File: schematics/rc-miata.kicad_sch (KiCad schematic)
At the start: 5 parts, among them M1 BLDC_MOTOR, U1 ESP32-C3-DevKitM-1, U2 UBEC, U3 ESC

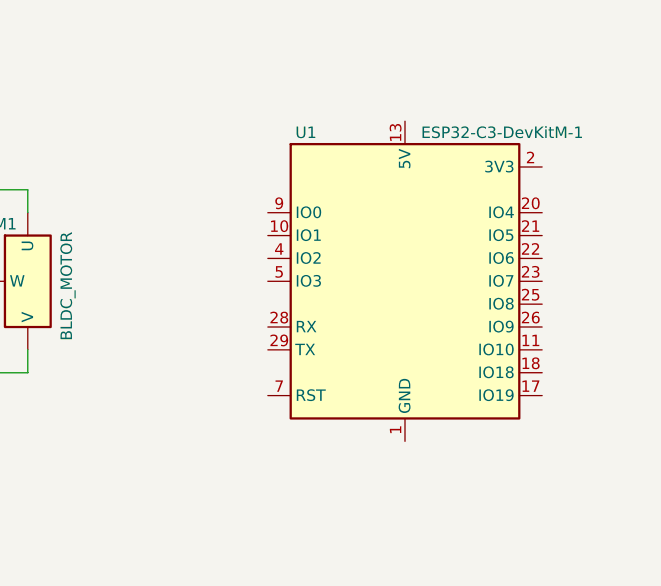
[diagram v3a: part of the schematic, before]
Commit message: Added 5V to ESP
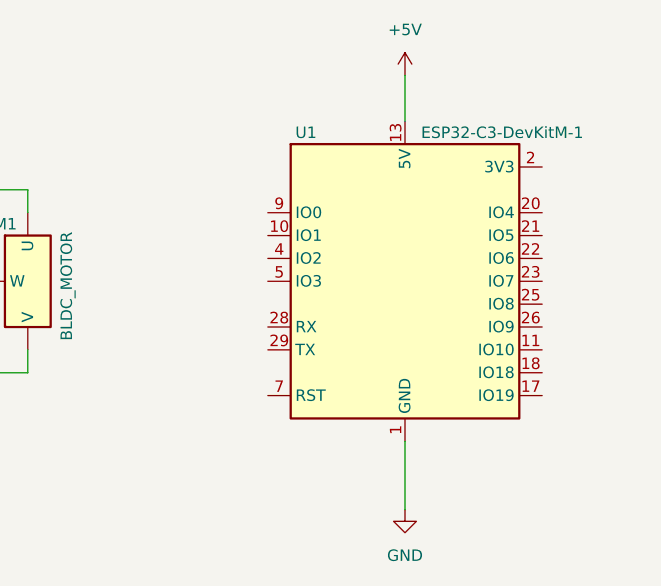
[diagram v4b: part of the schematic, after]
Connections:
- net +5V: now also U1.13 (5V), U1.14 (5V)
- net GND: now also U1.1 (GND), U1.12 (GND), U1.15 (GND), U1.16 (GND), U1.19 (GND), U1.24 (GND), U1.27 (GND), U1.30 (GND), U1.6 (GND), U1.8 (GND)
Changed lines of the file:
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@@
+	(wire
+		(pts
+			(xy 170.18 134.62) (xy 170.18 127)
+		)
+		(stroke
+			(width 0)
+			(type default)
+		)
+	)
 	(wire
 		(pts
@@
 		(pts
 			(xy 60.96 93.98) (xy 38.1 93.98)
+		)
+		(stroke
+			(width 0)
+			(type default)
+		)
+	)
+	(wire
+		(pts
+			(xy 170.18 86.36) (xy 170.18 91.44)
 		)
 		(stroke
@@
 	)
 	(symbol
+		(lib_id "power:GND")
+		(at 170.18 134.62 0)
+		(unit 1)
+		(body_style 1)
+		(exclude_from_sim no)
+		(in_bom yes)
+		(on_board yes)
+		(in_pos_files yes)
+		(dnp no)
+		(fields_autoplaced yes)
+		(property "Reference" "#PWR06"
+			(at 170.18 140.97 0)
+			(hide yes)
+			(show_name no)
+			(do_not_autoplace no)
+			(effects
+				(font
+					(size 1.27 1.27)
+				)
+			)
+		)
+		(property "Value" "GND"
+			(at 170.18 139.7 0)
+			(show_name no)
+			(do_not_autoplace no)
+			(effects
+				(font
+					(size 1.27 1.27)
+				)
+			)
+		)
+		(property "Footprint" ""
+			(at 170.18 134.62 0)
+			(hide yes)
+			(show_name no)
+			(do_not_autoplace no)
+			(effects
+				(font
+					(size 1.27 1.27)
+				)
+			)
+		)
+		(property "Datasheet" ""
+			(at 170.18 134.62 0)
+			(hide yes)
+			(show_name no)
+			(do_not_autoplace no)
+			(effects
+				(font
+					(size 1.27 1.27)
+				)
+			)
+		)
+		(property "Description" "Power symbol creates a global label with name \"GND\" , ground"
+			(at 170.18 134.62 0)
+			(hide yes)
+			(show_name no)
+			(do_not_autoplace no)
+			(effects
+				(font
+					(size 1.27 1.27)
+				)
+			)
+		)
+		(pin "1"
+		)
+		(instances
+			(project "rc-miata"
+				(path "/59cbdaad-7c89-4958-b9bb-08b035442600"
+					(reference "#PWR06")
+					(unit 1)
+				)
+			)
+		)
+	)
+	(symbol
 		(lib_id "RC Components:UBEC")
 		(at 58.42 101.6 0)
@@
 					(unit 1)
 				)
+			)
+		)
+	)
+	(symbol
+		(lib_id "power:+5V")
+		(at 170.18 86.36 0)
+		(unit 1)
+		(body_style 1)
+		(exclude_from_sim no)
+		(in_bom yes)
+		(on_board yes)
+		(in_pos_files yes)
+		(dnp no)
+		(fields_autoplaced yes)
+		(property "Reference" "#PWR05"
+			(at 170.18 90.17 0)
+			(hide yes)
+			(show_name no)
+			(do_not_autoplace no)
+			(effects
+				(font
+					(size 1.27 1.27)
+				)
+			)
+		)
+		(property "Value" "+5V"
+			(at 170.18 81.28 0)
+			(show_name no)
+			(do_not_autoplace no)
+			(effects
+				(font
+					(size 1.27 1.27)
+				)
+			)
+		)
+		(property "Footprint" ""
+			(at 170.18 86.36 0)
+			(hide yes)
+			(show_name no)
+			(do_not_autoplace no)
+			(effects
+				(font
+					(size 1.27 1.27)
+				)
+			)
+		)
+		(property "Datasheet" ""
+			(at 170.18 86.36 0)
+			(hide yes)
+			(show_name no)
+			(do_not_autoplace no)
+			(effects
+				(font
+					(size 1.27 1.27)
+				)
+			)
+		)
+		(property "Description" "Power symbol creates a global label with name \"+5V\""
+			(at 170.18 86.36 0)
+			(hide yes)
+			(show_name no)
+			(do_not_autoplace no)
+			(effects
+				(font
+					(size 1.27 1.27)
+				)
+			)
+		)
+		(pin "1"
+		)
+		(instances
+			(project "rc-miata"
+				(path "/59cbdaad-7c89-4958-b9bb-08b035442600"
+					(reference "#PWR05")
+					(unit 1)
+				)

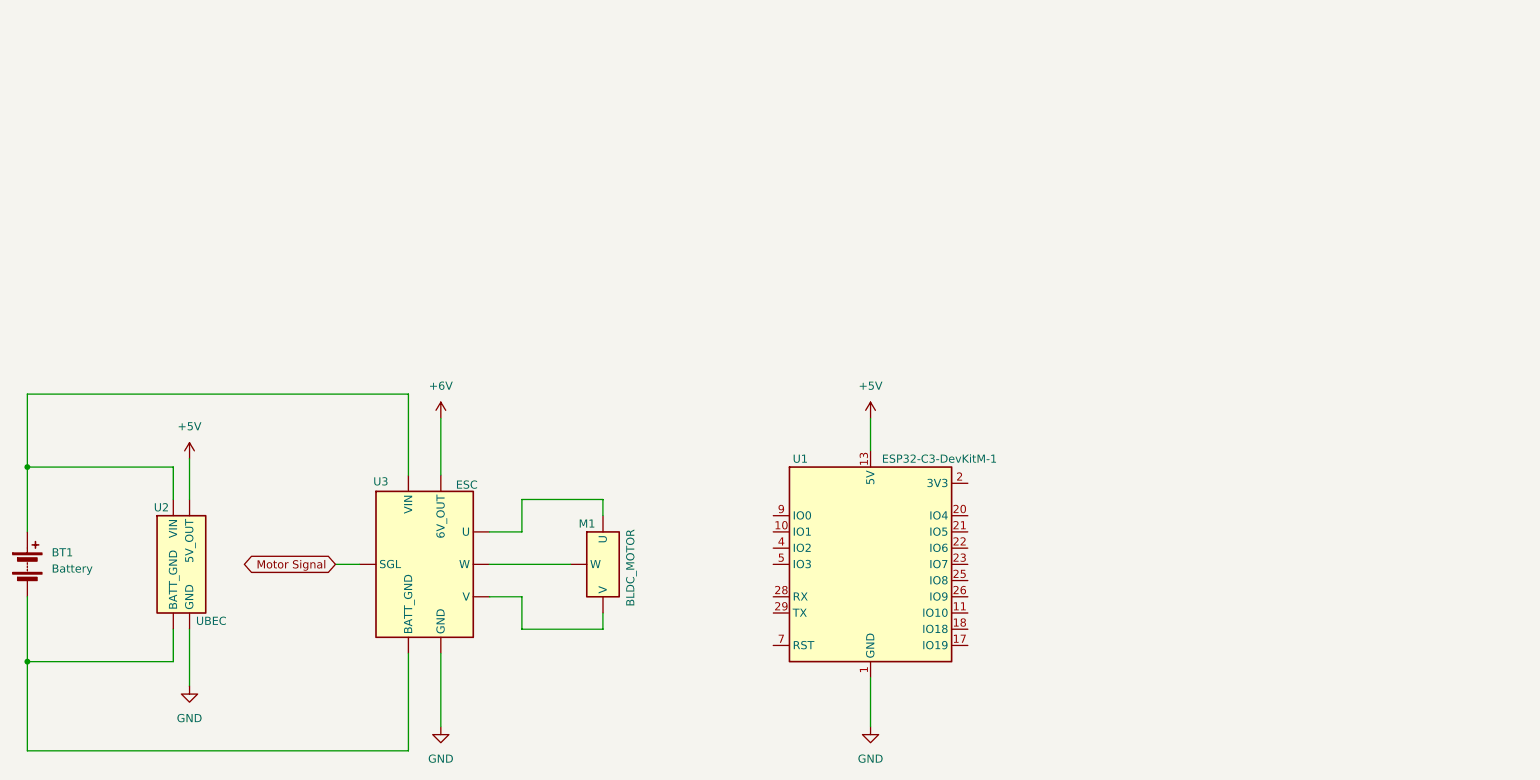
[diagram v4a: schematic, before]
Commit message: Named nets. Started updating ESP32
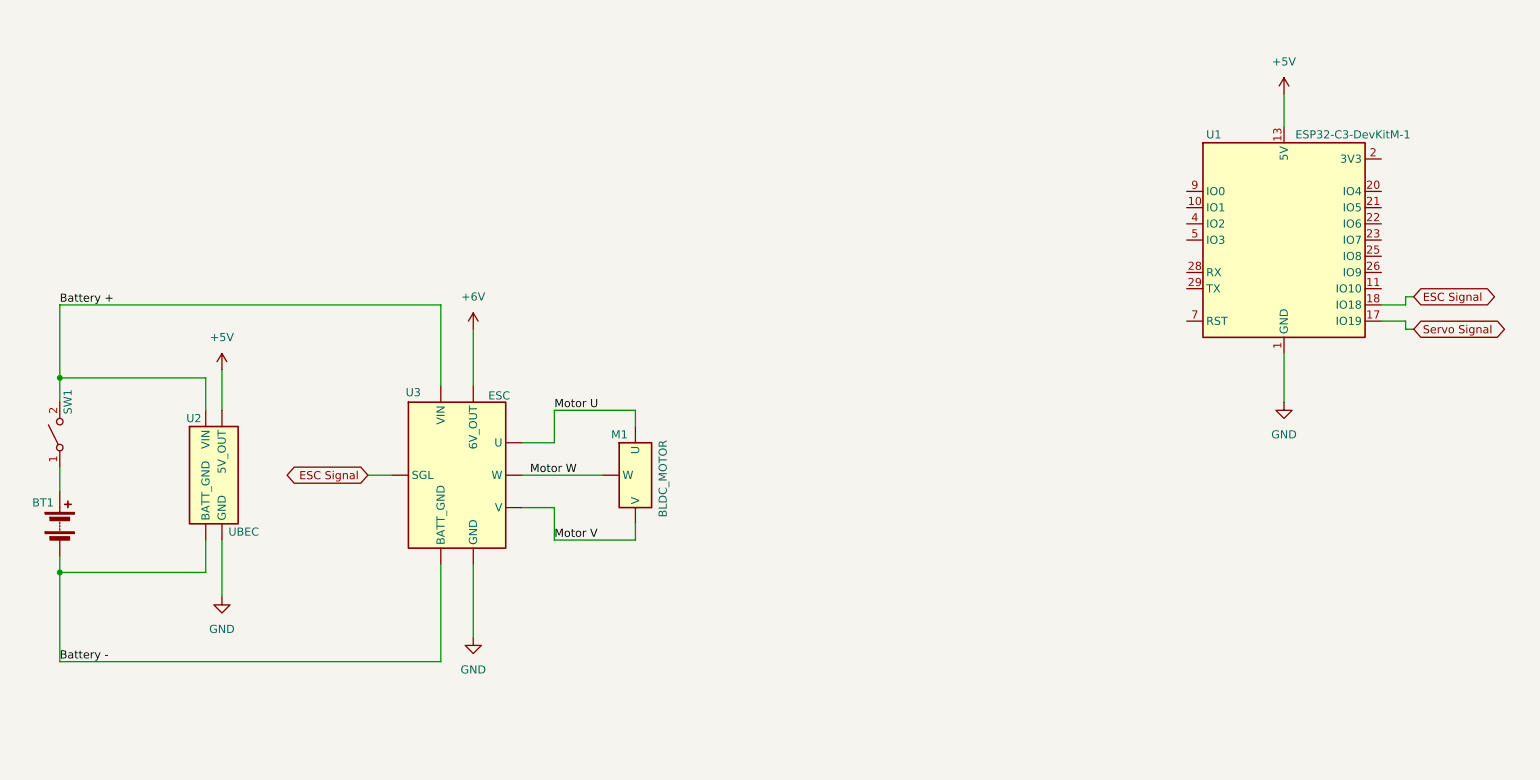
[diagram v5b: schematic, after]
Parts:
- added SW1: (no value), symbol Switch:SW_SPST
- BT1: value Battery -> 11.1
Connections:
- net Motor Signal is gone; now on net ESC Signal: U3.5 (SGL)
- net Servo Signal: now reaches U1.17 (IO19)
- net ESC Signal: now reaches U1.18 (IO18)
- net Motor U: now reaches M1.1 (U), U3.6 (U)
- net Motor V: now reaches M1.2 (V), U3.7 (V)
- net Motor W: now reaches M1.3 (W), U3.8 (W)
- net Battery +: now reaches U2.1 (VIN), U3.1 (VIN)
- net Battery +: now also SW1.2 (B); no longer BT1.1 (+)
- net Battery -: now reaches BT1.2 (-), U2.2 (BATT_GND), U3.2 (BATT_GND)
- new net: BT1.1 (+), SW1.1 (A)
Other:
- moved on the sheet: BT1, M1, U1, U2, U3

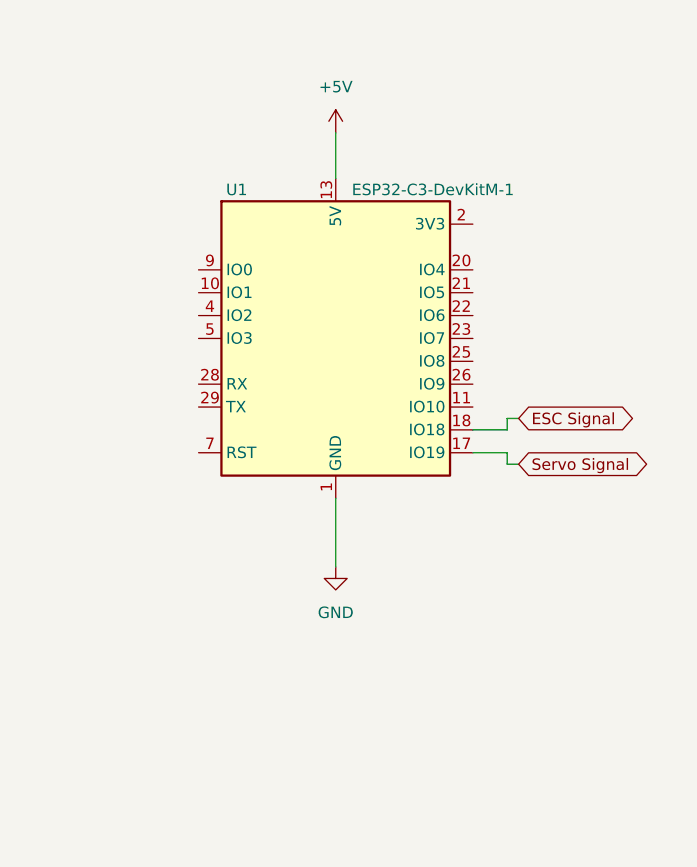
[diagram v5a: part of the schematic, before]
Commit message: Created ESP32 Symbol. Wired ESP32
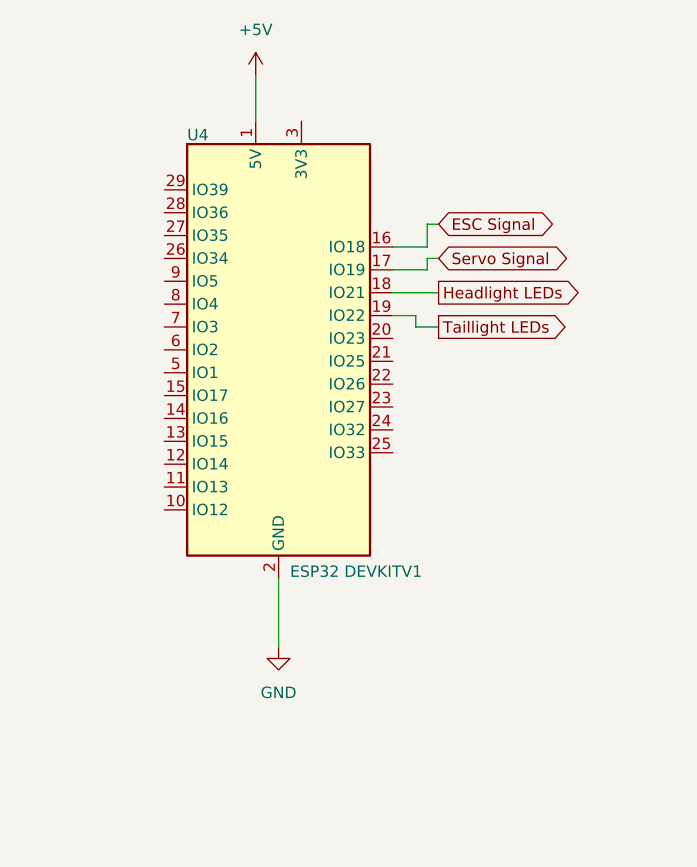
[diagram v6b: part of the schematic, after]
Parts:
- removed U1: ESP32-C3-DevKitM-1, RF_Module:ESP32-C3-DevKitM-1, symbol RF_Module:ESP32-C3-DevKitM-1
- added U4: ESP32 DEVKITV1, symbol ESP32s:ESP32_DEVKITV1
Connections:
- net +5V: now also U4.1 (5V)
- net ESC Signal: now also U4.16 (IO18)
- net GND: now also U4.2 (GND)
- net Servo Signal: now also U4.17 (IO19)
- new net Headlight LEDs: U4.18 (IO21)
- new net Taillight LEDs: U4.19 (IO22)

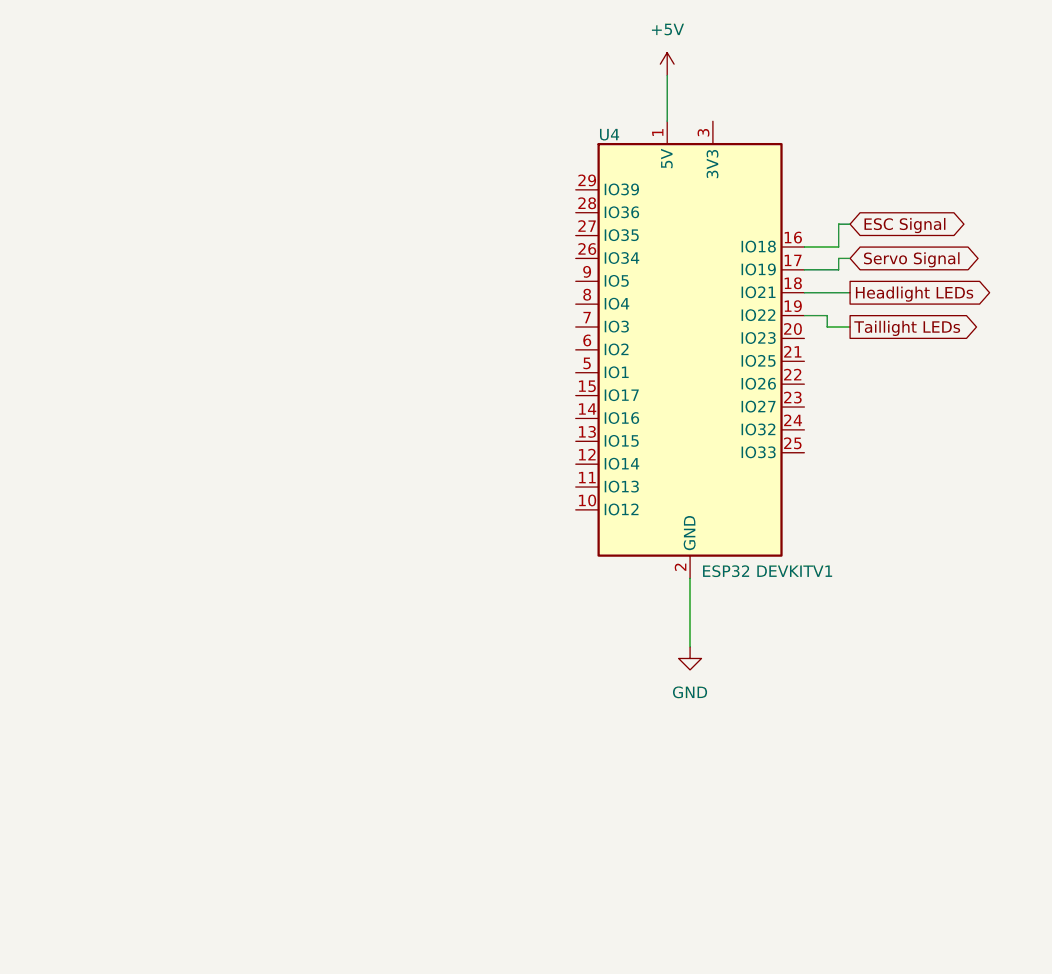
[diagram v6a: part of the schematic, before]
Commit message: Created Servo symbol. Wired servo.
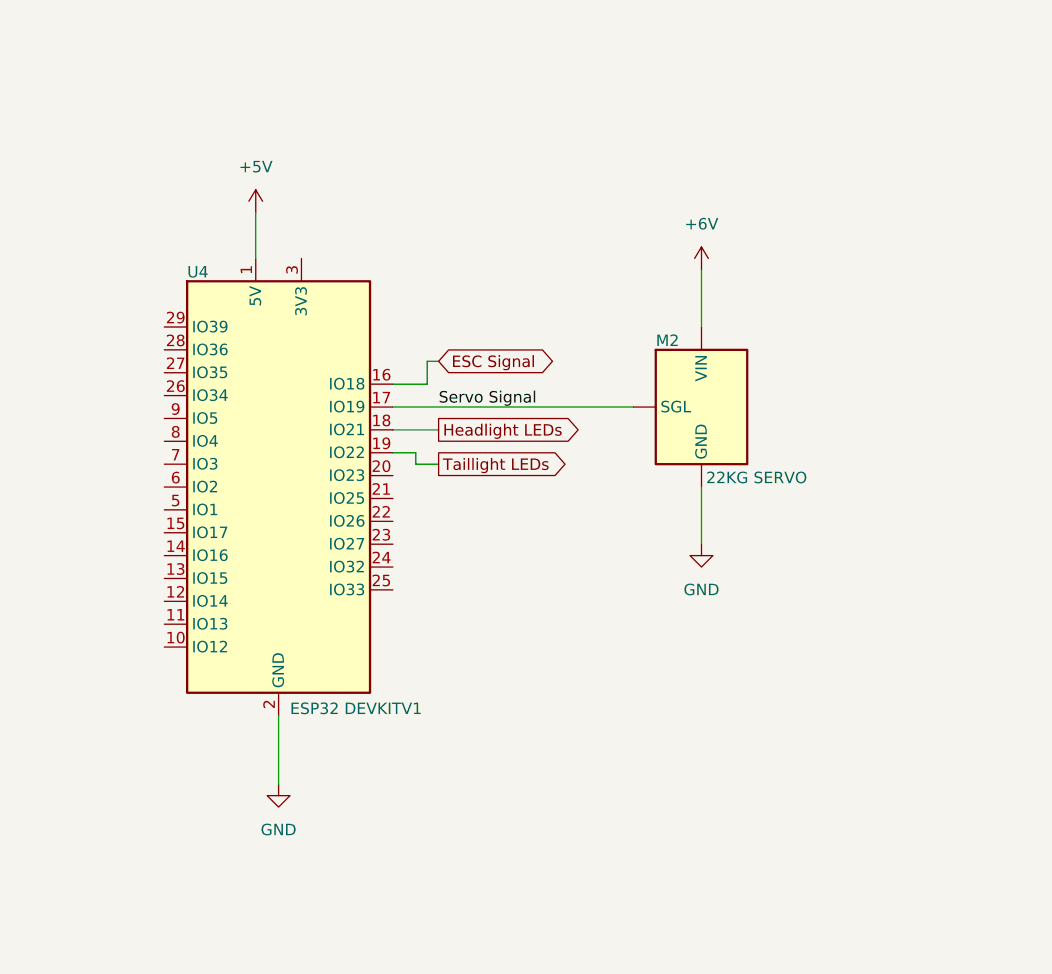
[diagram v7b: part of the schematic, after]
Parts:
- added M2: 22KG SERVO, symbol RC Components:SERVO
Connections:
- net +6V: now also M2.2 (VIN)
- net GND: now also M2.3 (GND)
- net Servo Signal: now also M2.1 (SGL)
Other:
- moved on the sheet: U4

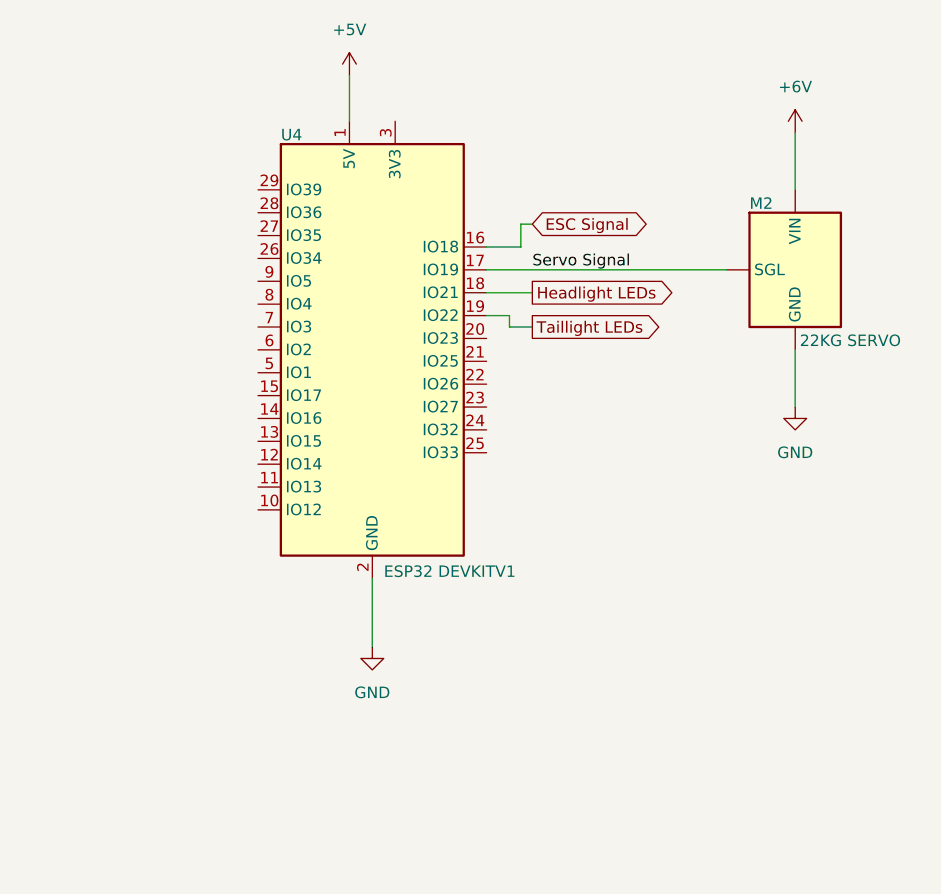
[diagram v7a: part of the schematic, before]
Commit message: Added decoupling capacitor
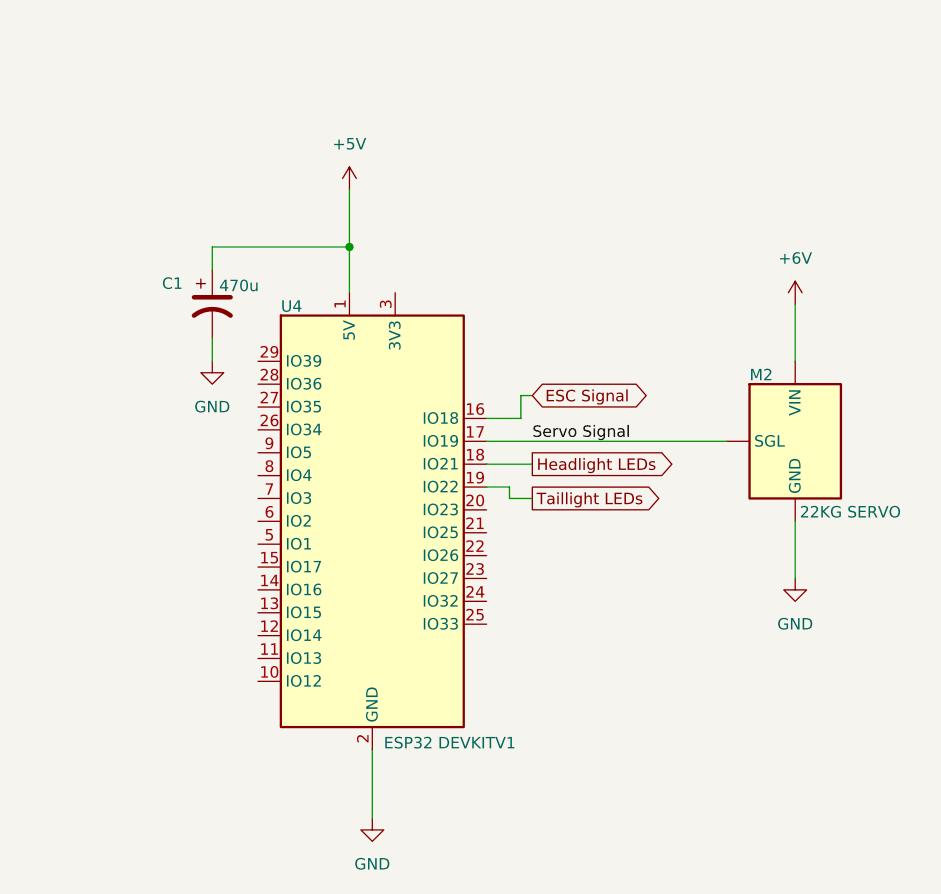
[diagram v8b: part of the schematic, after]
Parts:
- added C1: 470u, symbol Device:C_Polarized_US
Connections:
- net +5V: now also C1.1
- net GND: now also C1.2
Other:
- moved on the sheet: M2, U4
